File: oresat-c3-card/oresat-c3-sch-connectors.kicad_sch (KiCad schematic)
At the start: 24 parts, among them J1 TFM-120-01-L-D-RA, J3 733000020, J4 733000020, J8 SM14B-SHLS-TF

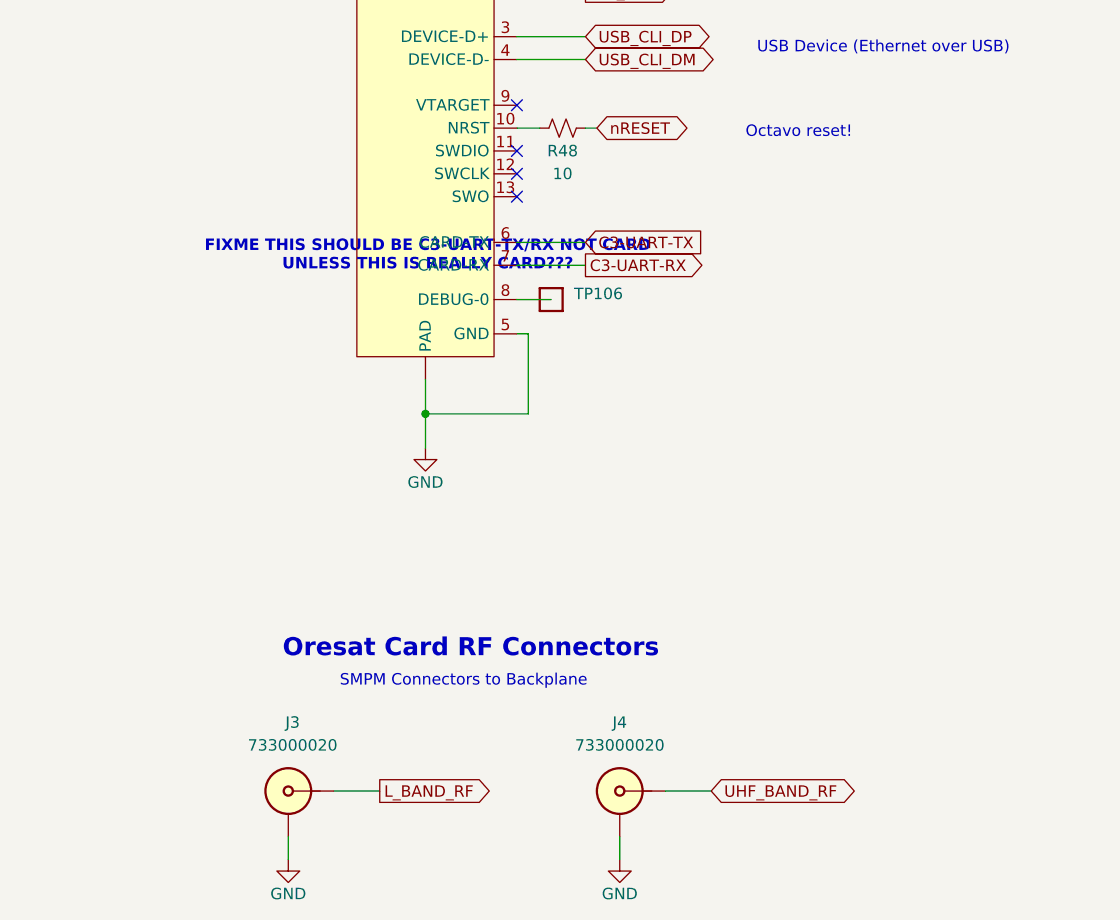
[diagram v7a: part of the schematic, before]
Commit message: Updating BOM and switching to oresat-passive footprints. Fixed some power cutoff limits, and fixed another DC voltage leverl on an LNA!
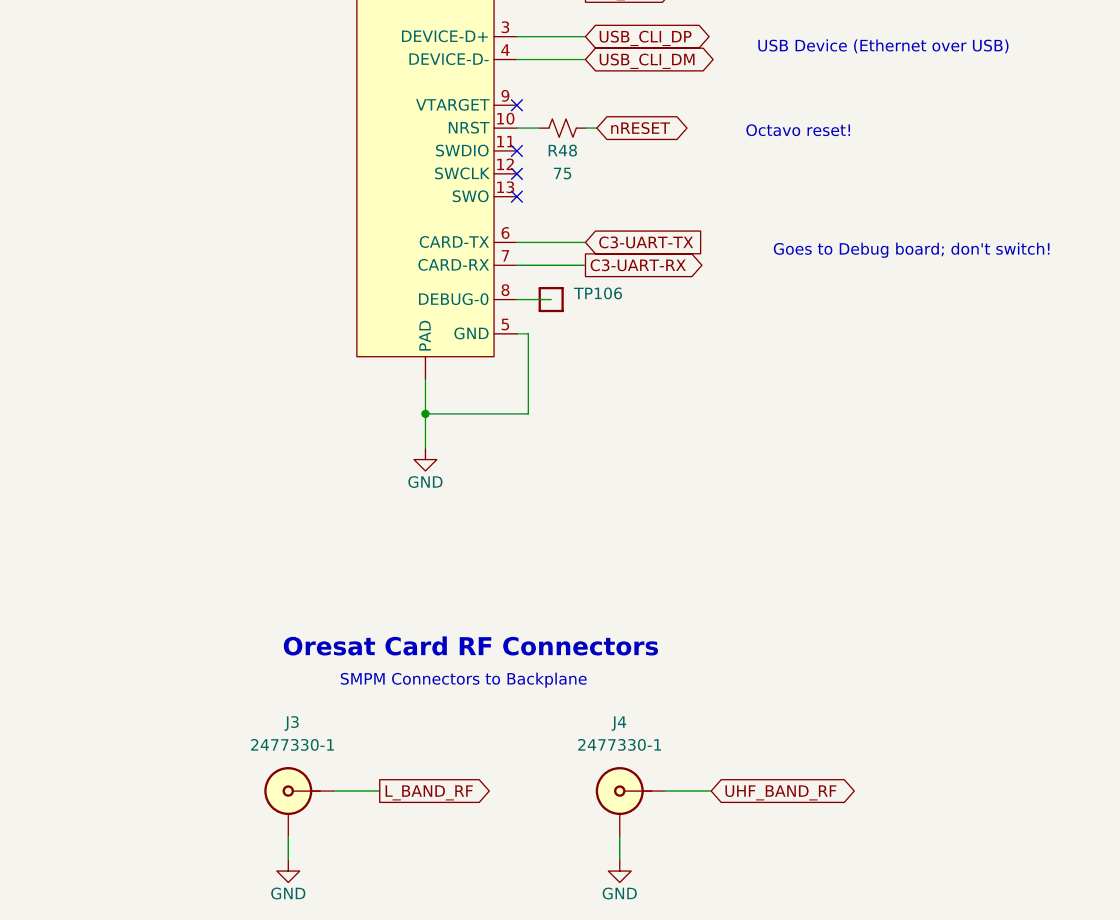
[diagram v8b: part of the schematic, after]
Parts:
- J1: DST Digi-Key -> DigiKey
- J3, J4: value 733000020 -> 2477330-1; DPN WM10772-ND -> 343-2477330-1CT-ND; DST Digi-Key -> DigiKey; MFR Molex -> TE Connectivity Linx; MPN 0733000020 -> 2477330-1
- PCB1: DPN (none) -> N/A; DST (none) -> N/A; MFR (none) -> N/A; MPN (none) -> N/A
- R48: value 10 -> 75; footprint Resistor_SMD:R_0603_1608Metric -> oresat-passives:0603-C-NOSILK; DPN RMCF0603FT10R0CT-ND -> RMCF0603FT75R0CT-ND; DST Digi-Key -> DigiKey; MPN RMCF0603FT10R0 -> RMCF1206FT75R0
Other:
- note added: "Goes to Debug board; don't switch!"
- note removed: "FIXME THIS SHOULD BE C3-UART-TX/RX NOT CARD UNLESS THIS IS REALLY CARD???"
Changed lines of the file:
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@@
+		)
+	)
+	(text "Goes to Debug board; don't switch!"
+		(exclude_from_sim no)
+		(at 266.192 101.346 0)
+		(effects
+			(font
+				(size 1.27 1.27)
+			)
 		)
 	)
@@
 			)
 			(justify left bottom)
-		)
-	)
-	(text "FIXME THIS SHOULD BE C3-UART-TX/RX NOT CARD\nUNLESS THIS IS REALLY CARD???"
-		(exclude_from_sim no)
-		(at 212.344 101.854 0)
-		(effects
-			(font
-				(size 1.27 1.27)
-				(thickness 0.254)
-				(bold yes)
-			)
 		)
 	)
@@
 			)
 		)
-		(property "Value" "733000020"
+		(property "Value" "2477330-1"
 			(at 197.3326 156.21 0)
 			(effects
@@
 			)
 		)
-		(property "Datasheet" "https://tools.molex.com/pdm_docs/sd/733000020_sd.pdf"
+		(property "Datasheet" "https://www.te.com/commerce/DocumentDelivery/DDEController?Action=srchrtrv&DocNm=SMPM_Connectors_Product_Extension-en&DocType=Data+Sheet&DocLang=English&DocFormat=pdf&PartCntxt=2477330-1"
 			(at 196.85 152.4 0)
 			(effects
@@
 			)
 		)
-		(property "Description" "Edge mounted SMPM 50ohm Connector"
+		(property "Description" "SMPM Connector Plug, Male Pin 50 Ohms Board Edge, Cutout; Surface Mount Solder"
 			(at 196.85 161.29 0)
 			(effects
@@
 			)
 		)
-		(property "DPN" "WM10772-ND"
+		(property "DPN" "343-2477330-1CT-ND"
 			(at 196.85 161.29 0)
 			(effects
@@
 			)
 		)
-		(property "DST" "Digi-Key"
+		(property "DST" "DigiKey"
 			(at 196.85 161.29 0)
 			(effects
@@
 			)
 		)
-		(property "MFR" "Molex"
+		(property "MFR" "TE Connectivity Linx"
 			(at 196.85 161.29 0)
 			(effects
@@
 			)
 		)
-		(property "MPN" "0733000020"
+		(property "MPN" "2477330-1"
 			(at 196.85 161.29 0)
 			(effects
@@
 			)
 		)
-		(property "Value" "10"
+		(property "Value" "75"
 			(at 227.33 92.71 90)
 			(effects
@@
 			)
 		)
-		(property "Footprint" "Resistor_SMD:R_0603_1608Metric"
+		(property "Footprint" "oresat-passives:0603-C-NOSILK"
 			(at 227.33 87.63 0)
 			(effects
@@
 			)
 		)
-		(property "Datasheet" "~"
+		(property "Datasheet" "https://www.seielect.com/catalog/SEI-RMCF_RMCP.pdf"
 			(at 227.33 87.63 0)
 			(effects
@@
 			)
 		)
-		(property "Description" "10 Ohms ±1% 0.1W, 1/10W Chip Resistor 0603 (1608 Metric) Automotive AEC-Q200 Thick Film"
+		(property "Description" "75 Ohms ±1% 0.1W, 1/10W Chip Resistor 0603 (1608 Metric) Automotive AEC-Q200 Thick Film"
 			(at 227.33 87.63 0)
 			(effects
@@
 			)
 		)
-		(property "DPN" "RMCF0603FT10R0CT-ND"
+		(property "DPN" "RMCF0603FT75R0CT-ND"
 			(at 227.33 87.63 0)
 			(effects
@@
 			)
 		)
-		(property "DST" "Digi-Key"
+		(property "DST" "DigiKey"
 			(at 227.33 87.63 0)
 			(effects
@@
 			)
 		)
-		(property "MPN" "RMCF0603FT10R0"
+		(property "MPN" "RMCF1206FT75R0"
 			(at 227.33 87.63 0)
 			(effects
@@
 			)
 		)
-		(property "Datasheet" ""
+		(property "Datasheet" "N/A"
 			(at 214.63 193.04 0)
 			(effects
@@
 			)
 		)
-		(property "Description" ""
+		(property "Description" "C3 v7.0 Card"
+			(at 214.63 193.04 0)
+			(effects
+				(font
+					(size 1.27 1.27)
+				)
+				(hide yes)
+			)
+		)
+		(property "DPN" "N/A"
+			(at 214.63 193.04 0)
+			(effects
+				(font
+					(size 1.27 1.27)
+				)
+				(hide yes)
+			)
+		)
+		(property "DST" "N/A"
+			(at 214.63 193.04 0)
+			(effects
+				(font
+					(size 1.27 1.27)
+				)
+				(hide yes)
+			)
+		)
+		(property "MFR" "N/A"
+			(at 214.63 193.04 0)
+			(effects
+				(font
+					(size 1.27 1.27)
+				)
+				(hide yes)
+			)
+		)
+		(property "MPN" "N/A"
 			(at 214.63 193.04 0)
 			(effects
@@
 			)
 		)
-		(property "Value" "733000020"
+		(property "Value" "2477330-1"
 			(at 233.68 156.21 0)
 			(effects
@@
 			)
 		)
-		(property "Datasheet" "https://tools.molex.com/pdm_docs/sd/733000020_sd.pdf"
+		(property "Datasheet" "https://www.te.com/commerce/DocumentDelivery/DDEController?Action=srchrtrv&DocNm=SMPM_Connectors_Product_Extension-en&DocType=Data+Sheet&DocLang=English&DocFormat=pdf&PartCntxt=2477330-1"
 			(at 233.68 152.4 0)
 			(effects
@@
 			)
 		)
-		(property "Description" "Edge mounted SMPM 50ohm Connector"
+		(property "Description" "SMPM Connector Plug, Male Pin 50 Ohms Board Edge, Cutout; Surface Mount Solder"
 			(at 233.68 161.29 0)
 			(effects
@@
 			)
 		)
-		(property "DPN" "WM10772-ND"
+		(property "DPN" "343-2477330-1CT-ND"
 			(at 233.68 161.29 0)
 			(effects
@@
 			)
 		)
-		(property "DST" "Digi-Key"
+		(property "DST" "DigiKey"
 			(at 233.68 161.29 0)
 			(effects
@@
 			)
 		)
-		(property "MFR" "Molex"
+		(property "MFR" "TE Connectivity Linx"
 			(at 233.68 161.29 0)
 			(effects
@@
 			)
 		)
-		(property "MPN" "0733000020"
+		(property "MPN" "2477330-1"
 			(at 233.68 161.29 0)
 			(effects
@@
 			)
 		)
-		(property "DST" "Digi-Key"
+		(property "DST" "DigiKey"
 			(at 107.95 144.78 0)
 			(effects
